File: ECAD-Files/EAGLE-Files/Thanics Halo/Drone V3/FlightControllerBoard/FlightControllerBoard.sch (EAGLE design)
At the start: 107 parts, among them J12 UE27AE54100, J4 UE27AE54100, J5 U.FL, J7 62674-301121ALF, J8 MICROSD, T1 ALT4532M, T2 ALT4532M, U3 MPL115A2, U4 NEO-M8, U7 PDDL2450, U8 74HC4053

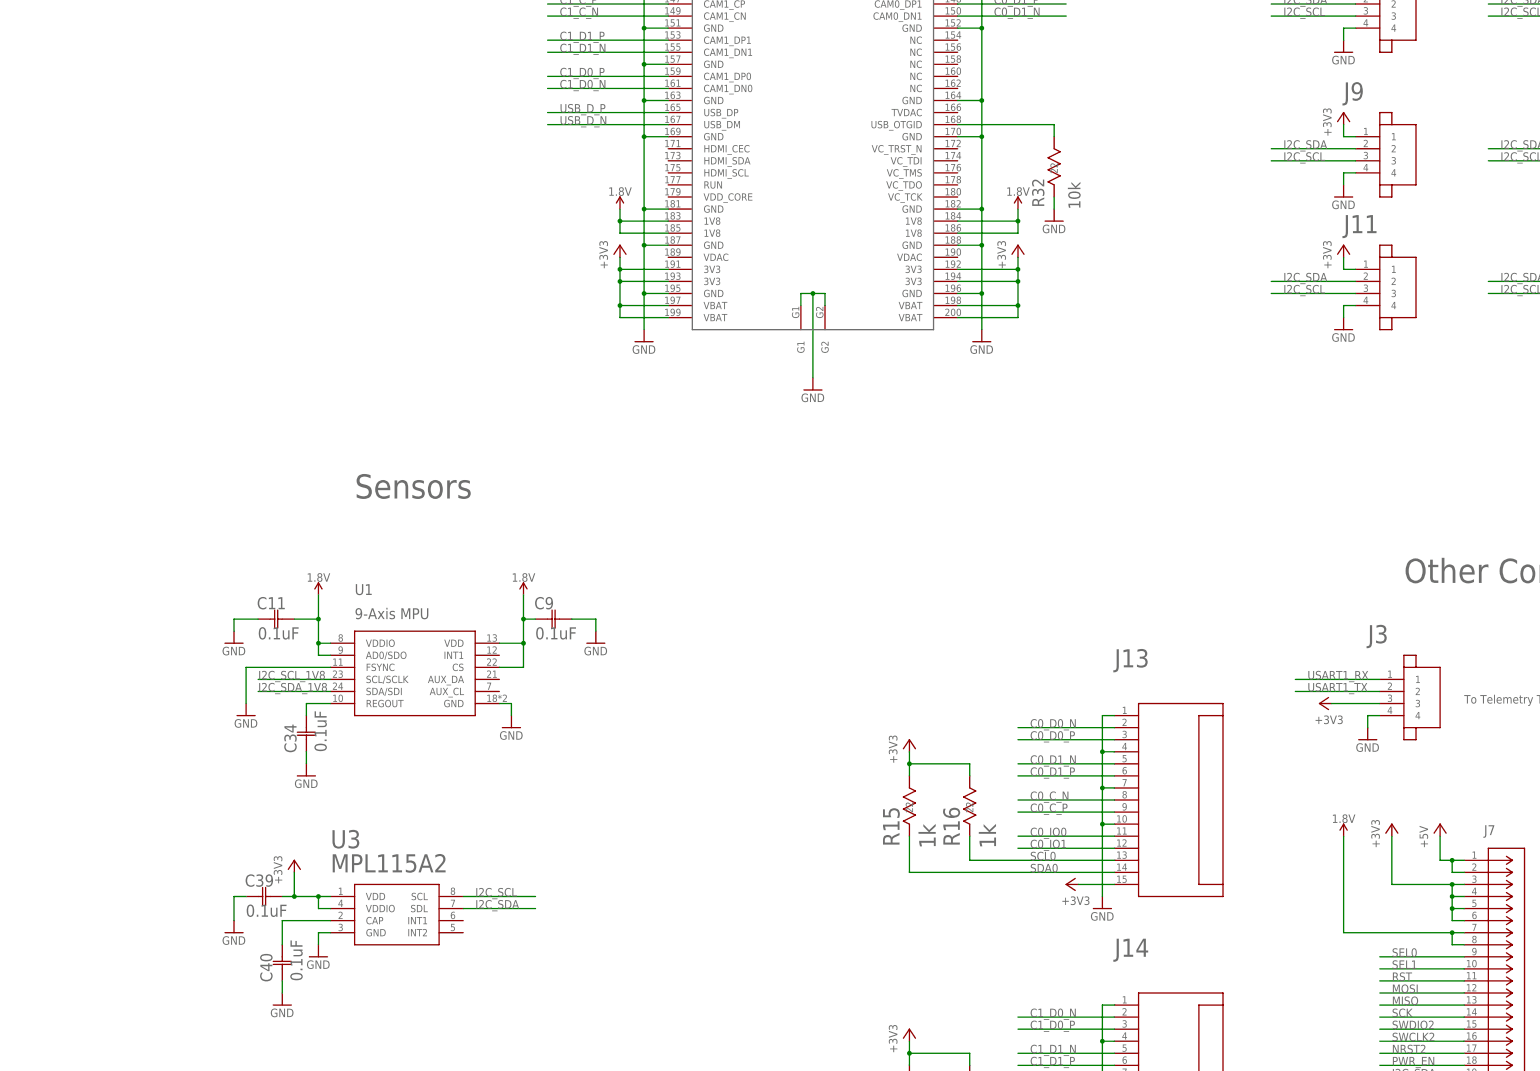
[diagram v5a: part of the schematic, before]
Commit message: Created TOF Altimeter Board v1, and made power board 4 layers
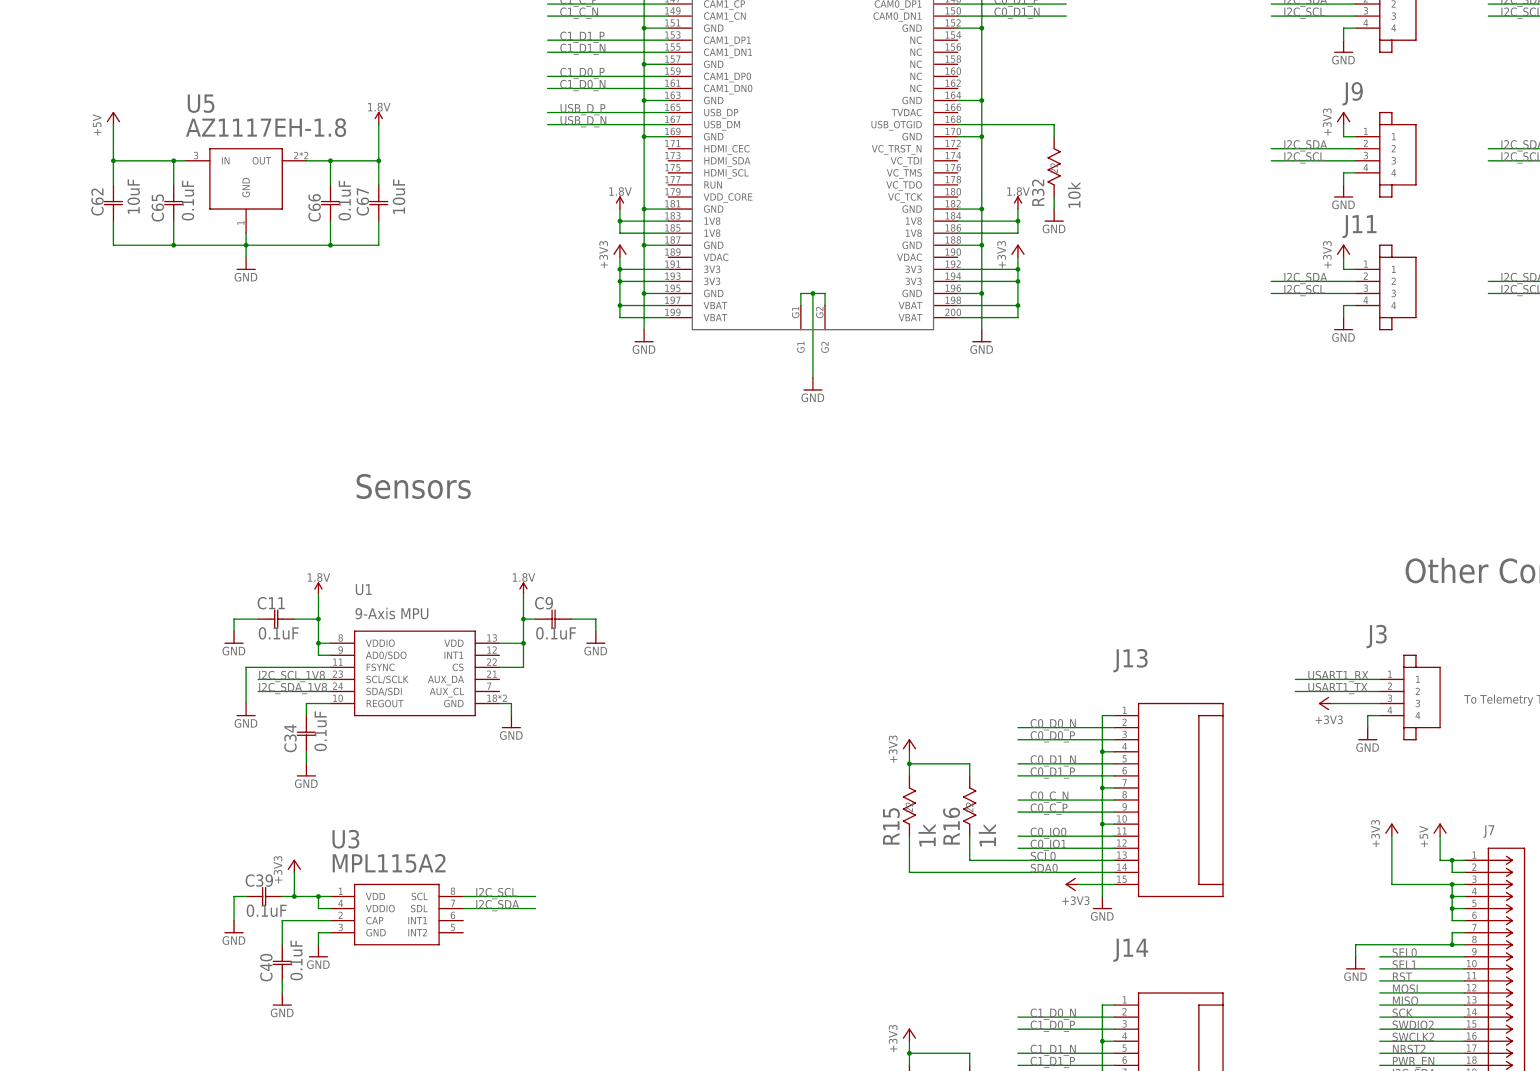
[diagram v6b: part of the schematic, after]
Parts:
- added C62, C67: 10uF, 10uF X5R Ceramic Capacitor:GRM21BR60J106ME19L
- added C65, C66: 0.1uF, 0.1uF-capacitor-0402:0402ZD104KAT2A0402-M
- added U5: AZ1117EH-1.8, thanics_robotics:AZ1117EH-1.8
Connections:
- net +5V: now also C62.22, C65.2, U5.IN
- net 1.8V: now also C66.2, C67.22, U5.OUT; no longer J7.77, J7.88
- net GND: now also C62.11, C65.1, C66.1, C67.11, J7.77, J7.88, U5.GND
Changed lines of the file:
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@@
 <part name="U7" library="thanics_robotics" deviceset="PDDL2450" device=""/>
 <part name="GND11" library="supply1" deviceset="GND" device=""/>
-<part name="SUPPLY5" library="SparkFun-PowerSymbols" deviceset="1.8V" device=""/>
 <part name="U3" library="mpl115a1-barometer" deviceset="MPL115A2" device=""/>
 <part name="+3V25" library="supply1" deviceset="+3V3" device=""/>
@@
 <part name="GND26" library="supply1" deviceset="GND" device=""/>
 <part name="GND56" library="supply1" deviceset="GND" device=""/>
+<part name="U5" library="thanics_robotics" deviceset="AZ1117EH-1.8" device=""/>
+<part name="GND133" library="supply1" deviceset="GND" device=""/>
+<part name="C62" library="10uF X5R Ceramic Capacitor" deviceset="GRM21BR60J106ME19L" device="" value="10uF"/>
+<part name="C65" library="0.1uF-capacitor-0402" deviceset="0402ZD104KAT2A" device="0402-M" value="0.1uF"/>
+<part name="C66" library="0.1uF-capacitor-0402" deviceset="0402ZD104KAT2A" device="0402-M" value="0.1uF"/>
+<part name="C67" library="10uF X5R Ceramic Capacitor" deviceset="GRM21BR60J106ME19L" device="" value="10uF"/>
+<part name="P+4" library="supply1" deviceset="+5V" device=""/>
+<part name="SUPPLY5" library="SparkFun-PowerSymbols" deviceset="1.8V" device=""/>
+<part name="GND79" library="supply1" deviceset="GND" device=""/>
 </parts>
 <sheets>
@@
 <instance part="U7" gate="G$1" x="-314.96" y="25.4"/>
 <instance part="GND11" gate="1" x="-281.94" y="66.04"/>
-<instance part="SUPPLY5" gate="G$1" x="109.22" y="-226.06"/>
 <instance part="U3" gate="G$1" x="-91.44" y="-243.84"/>
 <instance part="+3V25" gate="G$1" x="-111.76" y="-231.14"/>
@@
 <instance part="GND26" gate="1" x="365.76" y="-289.56"/>
 <instance part="GND56" gate="1" x="142.24" y="30.48"/>
+<instance part="U5" gate="G$1" x="-121.92" y="-88.9"/>
+<instance part="GND133" gate="1" x="-121.92" y="-106.68"/>
+<instance part="C62" gate="A" x="-149.86" y="-96.52" rot="R90"/>
+<instance part="C65" gate="A" x="-137.16" y="-96.52" rot="R90"/>
+<instance part="C66" gate="A" x="-104.14" y="-96.52" rot="R90"/>
+<instance part="C67" gate="A" x="-93.98" y="-96.52" rot="R90"/>
+<instance part="P+4" gate="1" x="-149.86" y="-73.66"/>
+<instance part="SUPPLY5" gate="G$1" x="-93.98" y="-76.2"/>
+<instance part="GND79" gate="1" x="111.76" y="-254"/>
 </instances>
 <busses>
@@
 <wire x1="142.24" y1="35.56" x2="142.24" y2="33.02" width="0.1524" layer="91"/>
 </segment>
+<segment>
+<pinref part="U5" gate="G$1" pin="GND"/>
+<pinref part="GND133" gate="1" pin="GND"/>
+<wire x1="-121.92" y1="-99.06" x2="-121.92" y2="-101.6" width="0.1524" layer="91"/>
+<pinref part="C65" gate="A" pin="1"/>
+<wire x1="-121.92" y1="-101.6" x2="-121.92" y2="-104.14" width="0.1524" layer="91"/>
+<wire x1="-137.16" y1="-96.52" x2="-137.16" y2="-101.6" width="0.1524" layer="91"/>
+<wire x1="-137.16" y1="-101.6" x2="-121.92" y2="-101.6" width="0.1524" layer="91"/>
+<junction x="-121.92" y="-101.6"/>
+<pinref part="C62" gate="A" pin="11"/>
+<wire x1="-137.16" y1="-101.6" x2="-149.86" y2="-101.6" width="0.1524" layer="91"/>
+<wire x1="-149.86" y1="-101.6" x2="-149.86" y2="-96.52" width="0.1524" layer="91"/>
+<junction x="-137.16" y="-101.6"/>
+<pinref part="C66" gate="A" pin="1"/>
+<wire x1="-121.92" y1="-101.6" x2="-104.14" y2="-101.6" width="0.1524" layer="91"/>
+<wire x1="-104.14" y1="-101.6" x2="-104.14" y2="-96.52" width="0.1524" layer="91"/>
+<pinref part="C67" gate="A" pin="11"/>
+<wire x1="-104.14" y1="-101.6" x2="-93.98" y2="-101.6" width="0.1524" layer="91"/>
+<wire x1="-93.98" y1="-101.6" x2="-93.98" y2="-96.52" width="0.1524" layer="91"/>
+<junction x="-104.14" y="-101.6"/>
+</segment>
+<segment>
+<pinref part="J7" gate="A" pin="88"/>
+<pinref part="GND79" gate="1" pin="GND"/>
+<wire x1="134.62" y1="-248.92" x2="132.08" y2="-248.92" width="0.1524" layer="91"/>
+<wire x1="132.08" y1="-248.92" x2="111.76" y2="-248.92" width="0.1524" layer="91"/>
+<wire x1="111.76" y1="-248.92" x2="111.76" y2="-251.46" width="0.1524" layer="91"/>
+<pinref part="J7" gate="A" pin="77"/>
+<wire x1="134.62" y1="-246.38" x2="132.08" y2="-246.38" width="0.1524" layer="91"/>
+<wire x1="132.08" y1="-246.38" x2="132.08" y2="-248.92" width="0.1524" layer="91"/>
+<junction x="132.08" y="-248.92"/>
+</segment>
 </net>
 <net name="N$1" class="0">
@@
 <wire x1="-241.3" y1="71.12" x2="-256.54" y2="71.12" width="0.1524" layer="91"/>
 <junction x="-256.54" y="71.12"/>
+</segment>
+<segment>
+<pinref part="P+4" gate="1" pin="+5V"/>
+<pinref part="C62" gate="A" pin="22"/>
+<wire x1="-149.86" y1="-76.2" x2="-149.86" y2="-83.82" width="0.1524" layer="91"/>
+<pinref part="U5" gate="G$1" pin="IN"/>
+<wire x1="-149.86" y1="-83.82" x2="-149.86" y2="-88.9" width="0.1524" layer="91"/>
+<wire x1="-134.62" y1="-83.82" x2="-137.16" y2="-83.82" width="0.1524" layer="91"/>
+<junction x="-149.86" y="-83.82"/>
+<pinref part="C65" gate="A" pin="2"/>
+<wire x1="-137.16" y1="-83.82" x2="-149.86" y2="-83.82" width="0.1524" layer="91"/>
+<wire x1="-137.16" y1="-88.9" x2="-137.16" y2="-83.82" width="0.1524" layer="91"/>
+<junction x="-137.16" y="-83.82"/>
 </segment>
 </net>
@@
 </segment>
 <segment>
-<wire x1="109.22" y1="-246.38" x2="109.22" y2="-226.06" width="0.1524" layer="91"/>
-<pinref part="J7" gate="A" pin="77"/>
-<wire x1="134.62" y1="-246.38" x2="132.08" y2="-246.38" width="0.1524" layer="91"/>
-<wire x1="132.08" y1="-246.38" x2="109.22" y2="-246.38" width="0.1524" layer="91"/>
-<wire x1="134.62" y1="-248.92" x2="132.08" y2="-248.92" width="0.1524" layer="91"/>
-<pinref part="J7" gate="A" pin="88"/>
-<wire x1="132.08" y1="-248.92" x2="132.08" y2="-246.38" width="0.1524" layer="91"/>
-<junction x="132.08" y="-246.38"/>
+<pinref part="U5" gate="G$1" pin="OUT"/>
+<pinref part="C66" gate="A" pin="2"/>
+<wire x1="-109.22" y1="-83.82" x2="-104.14" y2="-83.82" width="0.1524" layer="91"/>
+<wire x1="-104.14" y1="-83.82" x2="-104.14" y2="-88.9" width="0.1524" layer="91"/>
+<pinref part="C67" gate="A" pin="22"/>
+<wire x1="-104.14" y1="-83.82" x2="-93.98" y2="-83.82" width="0.1524" layer="91"/>
+<wire x1="-93.98" y1="-83.82" x2="-93.98" y2="-88.9" width="0.1524" layer="91"/>
+<junction x="-104.14" y="-83.82"/>
+<wire x1="-93.98" y1="-83.82" x2="-93.98" y2="-76.2" width="0.1524" layer="91"/>
+<junction x="-93.98" y="-83.82"/>
 <pinref part="SUPPLY5" gate="G$1" pin="1.8V"/>
 </segment>
